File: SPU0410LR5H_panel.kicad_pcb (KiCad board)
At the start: 2 copper layers, 70 x 35 mm, 168 parts, among them J1 Conn_01x04_Pin, U1 MCP6002-xSN, U2 SPU0410LR5H-QB

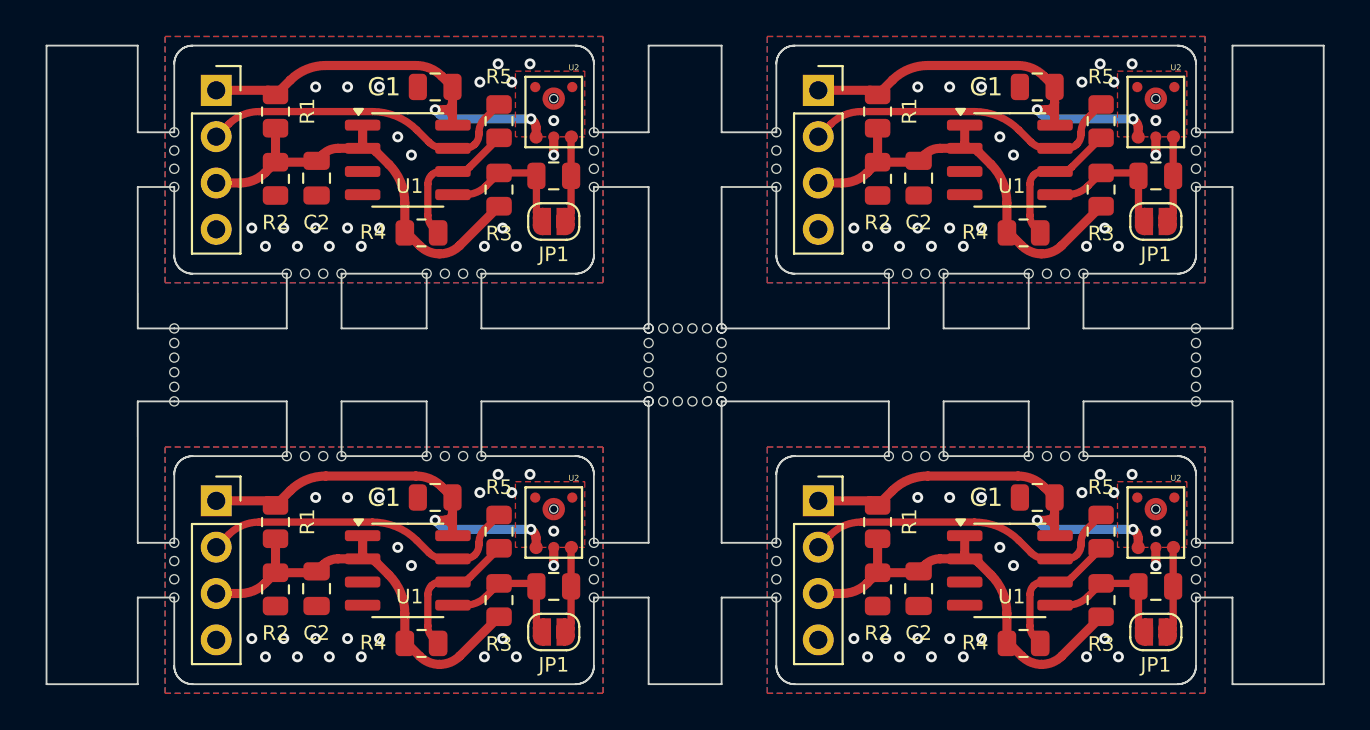
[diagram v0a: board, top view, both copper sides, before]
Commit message: silkscreen fix
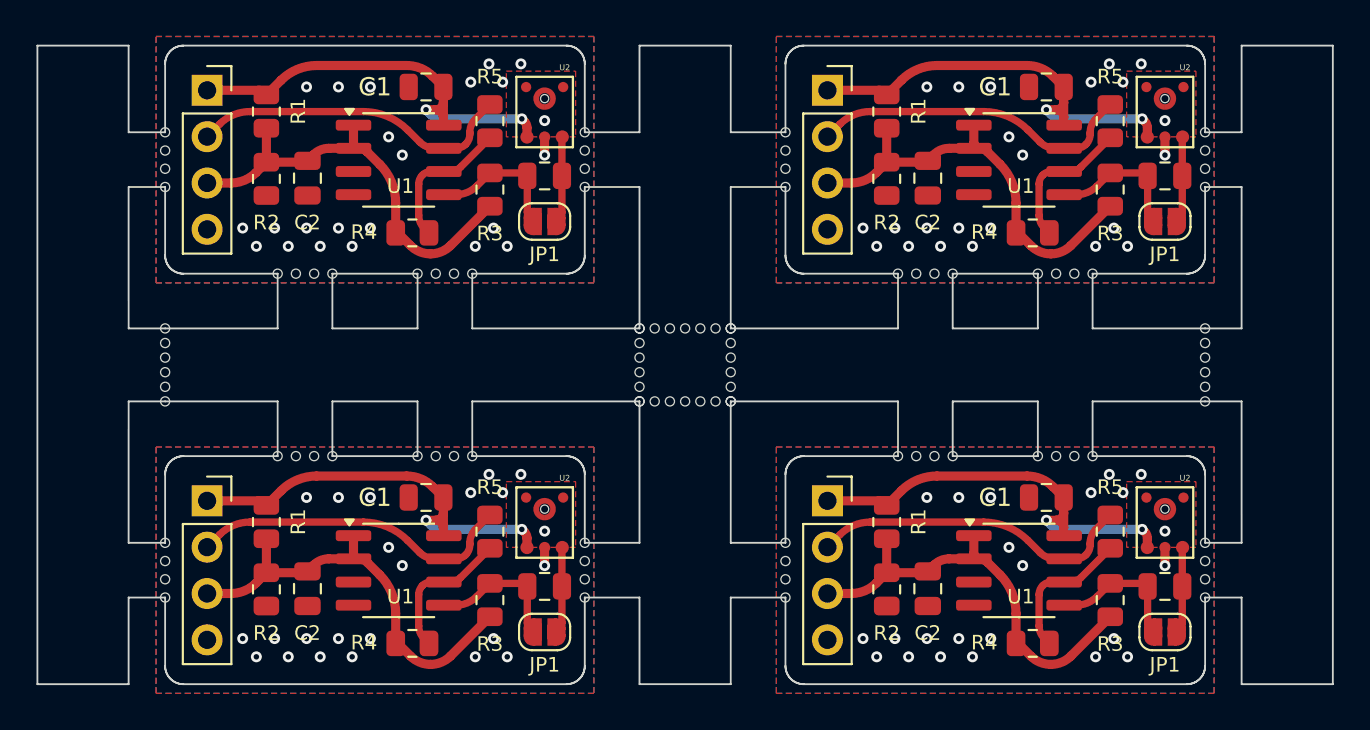
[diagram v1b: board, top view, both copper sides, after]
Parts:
- removed the C1 at (124.3, 22.3)
- removed the C1 at (91.3, 44.8)
- removed the C1 at (91.3, 22.3)
- removed the C1 at (124.3, 44.8)
- removed the C2 at (84.8, 27.3)
- removed the C2 at (84.8, 49.8)
- removed the C2 at (117.8, 49.8)
- removed the C2 at (117.8, 27.3)
- removed the C3 at (130.8, 27.1)
- removed the C3 at (97.8, 49.6)
- removed the C3 at (97.8, 27.1)
- removed the C3 at (130.8, 49.6)
- removed the G*** at (126.1, 24.9)
- removed the G*** at (126.1, 47.4)
- removed the G*** at (93.1, 24.9)
- removed the G*** at (93.1, 47.4)
- removed the J1 at (112.3, 45.0)
- removed the J1 at (79.3, 22.4)
- removed the J1 at (79.3, 45.0)
- removed the J1 at (112.3, 22.4)
- removed the JP1 at (97.8, 29.6)
- removed the JP1 at (130.8, 52.1)
- removed the JP1 at (97.8, 52.1)
- removed the JP1 at (130.8, 29.6)
- removed the R1 at (82.5, 23.6)
- removed the R1 at (82.5, 46.1)
- removed the R1 at (115.5, 23.6)
- removed the R1 at (115.5, 46.1)
- removed the R2 at (82.5, 49.8)
- removed the R2 at (115.5, 49.8)
- removed the R2 at (82.5, 27.3)
- removed the R2 at (115.5, 27.3)
- removed the R3 at (127.8, 27.9)
- removed the R3 at (94.8, 50.4)
- removed the R3 at (127.8, 50.4)
- removed the R3 at (94.8, 27.9)
- removed the R4 at (123.5, 52.8)
- removed the R4 at (90.5, 30.3)
- removed the R4 at (123.5, 30.3)
- removed the R4 at (90.5, 52.8)
- removed the R5 at (127.8, 46.6)
- removed the R5 at (94.8, 24.1)
- removed the R5 at (94.8, 46.6)
- removed the R5 at (127.8, 24.1)
- removed the U1 at (122.8, 26.3)
- removed the U1 at (122.8, 48.8)
- removed the U1 at (89.8, 48.8)
- removed the U1 at (89.8, 26.3)
- removed the U2 at (97.8, 23.6)
- removed the U2 at (97.8, 46.1)
- removed the U2 at (130.8, 23.6)
- removed the U2 at (130.8, 46.1)
- removed the kibuzzard-670AB1E7 at (84.0, 30.0)
- removed the kibuzzard-670AB1E7 at (117.0, 52.5)
- removed the kibuzzard-670AB1E7 at (84.0, 52.5)
- removed the kibuzzard-670AB1E7 at (117.0, 30.0)
- removed the kibuzzard-670AB1F3 at (117.5, 27.5)
- removed the kibuzzard-670AB1F3 at (117.5, 50.0)
- removed the kibuzzard-670AB1F3 at (84.5, 50.0)
- removed the kibuzzard-670AB1F3 at (84.5, 27.5)
- removed the kibuzzard-670AB201 at (84.2, 47.5)
- removed the kibuzzard-670AB201 at (117.2, 25.0)
- removed the kibuzzard-670AB201 at (84.2, 25.0)
- removed the kibuzzard-670AB201 at (117.2, 47.5)
- removed the kibuzzard-670AB20C at (85.3, 44.9)
- removed the kibuzzard-670AB20C at (118.3, 22.4)
- removed the kibuzzard-670AB20C at (85.3, 22.4)
- removed the kibuzzard-670AB20C at (118.3, 44.9)
- added C1: 1u, Capacitor_SMD:C_0805_2012Metric, F.Cu at (90.8, 44.8)
- added C1: 1u, Capacitor_SMD:C_0805_2012Metric, F.Cu at (124.8, 44.8)
- added C1: 1u, Capacitor_SMD:C_0805_2012Metric, F.Cu at (90.8, 22.3)
- added C1: 1u, Capacitor_SMD:C_0805_2012Metric, F.Cu at (124.8, 22.3)
- added C2: 1u, Capacitor_SMD:C_0805_2012Metric, F.Cu at (84.3, 49.8)
- added C2: 1u, Capacitor_SMD:C_0805_2012Metric, F.Cu at (118.3, 27.3)
- added C2: 1u, Capacitor_SMD:C_0805_2012Metric, F.Cu at (84.3, 27.3)
- added C2: 1u, Capacitor_SMD:C_0805_2012Metric, F.Cu at (118.3, 49.8)
- added C3: 68n, Capacitor_SMD:C_0805_2012Metric, F.Cu at (131.3, 27.1)
- added C3: 68n, Capacitor_SMD:C_0805_2012Metric, F.Cu at (97.3, 49.6)
- added C3: 68n, Capacitor_SMD:C_0805_2012Metric, F.Cu at (97.3, 27.1)
- added C3: 68n, Capacitor_SMD:C_0805_2012Metric, F.Cu at (131.3, 49.6)
- added G***: LOGO, LOGO, B.Cu at (126.6, 24.9)
- added G***: LOGO, LOGO, B.Cu at (126.6, 47.4)
- added G***: LOGO, LOGO, B.Cu at (92.6, 47.4)
- added G***: LOGO, LOGO, B.Cu at (92.6, 24.9)
- added J1: Conn_01x04_Pin, Connector_PinSocket_2.54mm:PinSocket_1x04_P2.54mm_Vertical, F.Cu at (112.8, 45.0)
- added J1: Conn_01x04_Pin, Connector_PinSocket_2.54mm:PinSocket_1x04_P2.54mm_Vertical, F.Cu at (78.8, 45.0)
- added J1: Conn_01x04_Pin, Connector_PinSocket_2.54mm:PinSocket_1x04_P2.54mm_Vertical, F.Cu at (78.8, 22.4)
- added J1: Conn_01x04_Pin, Connector_PinSocket_2.54mm:PinSocket_1x04_P2.54mm_Vertical, F.Cu at (112.8, 22.4)
- added JP1: SolderJumper_2_Open, Jumper:SolderJumper-2_P1.3mm_Open_RoundedPad1.0x1.5mm, F.Cu at (97.3, 52.1)
- added JP1: SolderJumper_2_Open, Jumper:SolderJumper-2_P1.3mm_Open_RoundedPad1.0x1.5mm, F.Cu at (97.3, 29.6)
- added JP1: SolderJumper_2_Open, Jumper:SolderJumper-2_P1.3mm_Open_RoundedPad1.0x1.5mm, F.Cu at (131.3, 52.1)
- added JP1: SolderJumper_2_Open, Jumper:SolderJumper-2_P1.3mm_Open_RoundedPad1.0x1.5mm, F.Cu at (131.3, 29.6)
- added KiKit_MB_21_7: NPTH, NPTH, F.Cu at (107.5, 39.5)
- added KiKit_MB_22_7: NPTH, NPTH, F.Cu at (102.5, 35.5)
- added R1: 10k, Resistor_SMD:R_0805_2012Metric, F.Cu at (82.0, 23.6)
- added R1: 10k, Resistor_SMD:R_0805_2012Metric, F.Cu at (116.0, 23.6)
- added R1: 10k, Resistor_SMD:R_0805_2012Metric, F.Cu at (82.0, 46.1)
- added R1: 10k, Resistor_SMD:R_0805_2012Metric, F.Cu at (116.0, 46.1)
- added R2: 10k, Resistor_SMD:R_0805_2012Metric, F.Cu at (116.0, 49.8)
- added R2: 10k, Resistor_SMD:R_0805_2012Metric, F.Cu at (116.0, 27.3)
- added R2: 10k, Resistor_SMD:R_0805_2012Metric, F.Cu at (82.0, 49.8)
- added R2: 10k, Resistor_SMD:R_0805_2012Metric, F.Cu at (82.0, 27.3)
- added R3: 100R, Resistor_SMD:R_0805_2012Metric, F.Cu at (94.3, 27.9)
- added R3: 100R, Resistor_SMD:R_0805_2012Metric, F.Cu at (128.3, 50.4)
- added R3: 100R, Resistor_SMD:R_0805_2012Metric, F.Cu at (94.3, 50.4)
- added R3: 100R, Resistor_SMD:R_0805_2012Metric, F.Cu at (128.3, 27.9)
- added R4: 330, Resistor_SMD:R_0805_2012Metric, F.Cu at (124.0, 52.8)
- added R4: 330, Resistor_SMD:R_0805_2012Metric, F.Cu at (124.0, 30.3)
- added R4: 330, Resistor_SMD:R_0805_2012Metric, F.Cu at (90.0, 30.3)
- added R4: 330, Resistor_SMD:R_0805_2012Metric, F.Cu at (90.0, 52.8)
- added R5: 470k, Resistor_SMD:R_0805_2012Metric, F.Cu at (128.3, 46.6)
- added R5: 470k, Resistor_SMD:R_0805_2012Metric, F.Cu at (128.3, 24.1)
- added R5: 470k, Resistor_SMD:R_0805_2012Metric, F.Cu at (94.3, 24.1)
- added R5: 470k, Resistor_SMD:R_0805_2012Metric, F.Cu at (94.3, 46.6)
- added U1: MCP6002-xSN, Package_SO:SOIC-8_3.9x4.9mm_P1.27mm, F.Cu at (89.3, 48.8)
- added U1: MCP6002-xSN, Package_SO:SOIC-8_3.9x4.9mm_P1.27mm, F.Cu at (123.3, 48.8)
- added U1: MCP6002-xSN, Package_SO:SOIC-8_3.9x4.9mm_P1.27mm, F.Cu at (89.3, 26.3)
- added U1: MCP6002-xSN, Package_SO:SOIC-8_3.9x4.9mm_P1.27mm, F.Cu at (123.3, 26.3)
- added U2: SPU0410LR5H-QB, SPU0410LR5H-QB:XDCR_SPU0410LR5H-QB, F.Cu at (97.3, 46.1)
- added U2: SPU0410LR5H-QB, SPU0410LR5H-QB:XDCR_SPU0410LR5H-QB, F.Cu at (97.3, 23.6)
- added U2: SPU0410LR5H-QB, SPU0410LR5H-QB:XDCR_SPU0410LR5H-QB, F.Cu at (131.3, 23.6)
- added U2: SPU0410LR5H-QB, SPU0410LR5H-QB:XDCR_SPU0410LR5H-QB, F.Cu at (131.3, 46.1)
- added kibuzzard-670AB1E7: G***, kibuzzard-670AB1E7, F.Cu at (117.5, 52.5)
- added kibuzzard-670AB1E7: G***, kibuzzard-670AB1E7, F.Cu at (83.5, 30.0)
- added kibuzzard-670AB1E7: G***, kibuzzard-670AB1E7, F.Cu at (83.5, 52.5)
- added kibuzzard-670AB1E7: G***, kibuzzard-670AB1E7, F.Cu at (117.5, 30.0)
- added kibuzzard-670AB1F3: G***, kibuzzard-670AB1F3, F.Cu at (118.0, 27.5)
- added kibuzzard-670AB1F3: G***, kibuzzard-670AB1F3, F.Cu at (118.0, 50.0)
- added kibuzzard-670AB1F3: G***, kibuzzard-670AB1F3, F.Cu at (84.0, 50.0)
- added kibuzzard-670AB1F3: G***, kibuzzard-670AB1F3, F.Cu at (84.0, 27.5)
- added kibuzzard-670AB201: G***, kibuzzard-670AB201, F.Cu at (117.7, 25.0)
- added kibuzzard-670AB201: G***, kibuzzard-670AB201, F.Cu at (83.7, 47.5)
- added kibuzzard-670AB201: G***, kibuzzard-670AB201, F.Cu at (83.7, 25.0)
- added kibuzzard-670AB201: G***, kibuzzard-670AB201, F.Cu at (117.7, 47.5)
- added kibuzzard-670AB20C: G***, kibuzzard-670AB20C, F.Cu at (118.8, 22.4)
- added kibuzzard-670AB20C: G***, kibuzzard-670AB20C, F.Cu at (84.8, 44.9)
- added kibuzzard-670AB20C: G***, kibuzzard-670AB20C, F.Cu at (84.8, 22.4)
- added kibuzzard-670AB20C: G***, kibuzzard-670AB20C, F.Cu at (118.8, 44.9)
- moved KiKit_MB_17_1 30.8 mm to (107.5, 39.5)
- moved KiKit_MB_17_6 30.8 mm to (107.5, 35.5)
- moved KiKit_MB_19_1 30.8 mm to (76.5, 35.5)
- moved KiKit_MB_19_6 30.8 mm to (76.5, 39.5)
- moved KiKit_MB_17_2 30.6 mm to (107.5, 38.7)
- moved KiKit_MB_17_5 30.6 mm to (107.5, 36.3)
- moved KiKit_MB_19_2 30.6 mm to (76.5, 36.3)
- moved KiKit_MB_19_5 30.6 mm to (76.5, 38.7)
- moved KiKit_MB_17_3 30.5 mm to (107.5, 37.9)
- moved KiKit_MB_17_4 30.5 mm to (107.5, 37.1)
- moved KiKit_MB_19_3 30.5 mm to (76.5, 37.1)
- moved KiKit_MB_19_4 30.5 mm to (76.5, 37.9)
- moved KiKit_MB_18_1 30.5 mm to (133.5, 35.5)
- moved KiKit_MB_18_2 30.5 mm to (133.5, 36.3)
- moved KiKit_MB_18_3 30.5 mm to (133.5, 37.1)
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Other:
- board size 70 x 35 mm -> 71 x 35 mm
- board text added: "SPU0410LR5H + HPF V1.2"
